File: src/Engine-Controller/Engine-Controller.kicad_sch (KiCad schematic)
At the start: 20 parts, among them J2 Jumper_NO, P3 3220-20-0200-00, U1 STM32H750VBTx, Y1 ECS-240-18-33-JGN-TR

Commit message: routed rev4
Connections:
- net NOZ_CONT: now also U1.38 (PE8); no longer U1.39 (PE9)
- net SP_CONT: now also U1.39 (PE9); no longer U1.38 (PE8)
- net SWCLK: now also R18.1
- net SWDIO: no longer R18.1
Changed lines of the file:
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@@
   (junction (at 248.285 140.97) (diameter 0) (color 0 0 0 0)
   )
+  (junction (at 201.295 117.475) (diameter 0) (color 0 0 0 0)
+  )
   (junction (at 204.47 145.415) (diameter 0) (color 0 0 0 0)
-  )
-  (junction (at 201.295 112.395) (diameter 0) (color 0 0 0 0)
   )
   (junction (at 32.385 41.91) (diameter 0) (color 0 0 0 0)
@@
     (stroke (width 0) (type default) (color 0 0 0 0))
   )
+  (wire (pts (xy 91.44 62.23) (xy 95.25 62.23))
+    (stroke (width 0) (type default) (color 0 0 0 0))
+  )
   (wire (pts (xy 91.44 39.37) (xy 95.25 39.37))
     (stroke (width 0) (type default) (color 0 0 0 0))
@@
     (stroke (width 0) (type default) (color 0 0 0 0))
   )
+  (wire (pts (xy 201.295 117.475) (xy 191.135 117.475))
+    (stroke (width 0) (type default) (color 0 0 0 0))
+  )
   (wire (pts (xy 31.115 127) (xy 34.29 127))
     (stroke (width 0) (type default) (color 0 0 0 0))
   )
-  (wire (pts (xy 91.44 62.23) (xy 95.25 62.23))
-    (stroke (width 0) (type default) (color 0 0 0 0))
-  )
   (polyline (pts (xy 172.085 116.205) (xy 115.57 116.205))
     (stroke (width 0) (type default) (color 0 0 0 0))
@@
     (stroke (width 0) (type default) (color 0 0 0 0))
   )
-  (wire (pts (xy 201.295 109.22) (xy 201.295 112.395))
+  (wire (pts (xy 91.44 59.69) (xy 95.25 59.69))
     (stroke (width 0) (type default) (color 0 0 0 0))
   )
@@
     (stroke (width 0) (type default) (color 0 0 0 0))
   )
-  (wire (pts (xy 207.01 112.395) (xy 201.295 112.395))
+  (wire (pts (xy 193.04 112.395) (xy 207.01 112.395))
     (stroke (width 0) (type default) (color 0 0 0 0))
   )
@@
     (stroke (width 0) (type default) (color 0 0 0 0))
   )
+  (wire (pts (xy 201.295 109.22) (xy 201.295 117.475))
+    (stroke (width 0) (type default) (color 0 0 0 0))
+  )
   (wire (pts (xy 32.385 46.99) (xy 32.385 49.53))
     (stroke (width 0) (type default) (color 0 0 0 0))
@@
     (stroke (width 0) (type default) (color 0 0 0 0))
   )
-  (wire (pts (xy 201.295 112.395) (xy 193.04 112.395))
-    (stroke (width 0) (type default) (color 0 0 0 0))
-  )
   (wire (pts (xy 91.44 69.85) (xy 95.25 69.85))
     (stroke (width 0) (type default) (color 0 0 0 0))
@@
     (stroke (width 0) (type default) (color 0 0 0 0))
   )
-  (wire (pts (xy 91.44 59.69) (xy 95.25 59.69))
-    (stroke (width 0) (type default) (color 0 0 0 0))
-  )
   (wire (pts (xy 31.115 74.93) (xy 34.29 74.93))
     (stroke (width 0) (type default) (color 0 0 0 0))
@@
     (stroke (width 0) (type default) (color 0 0 0 0))
   )
-  (wire (pts (xy 207.01 117.475) (xy 191.135 117.475))
+  (wire (pts (xy 207.01 117.475) (xy 201.295 117.475))
     (stroke (width 0) (type default) (color 0 0 0 0))
   )
@@
     )
   )
-  (global_label "SP_CONT" (shape input) (at 95.25 59.69 0) (fields_autoplaced)
-    (effects (font (size 1.27 1.27)) (justify left))
-    (property "Intersheet References" "${INTERSHEET_REFS}" (id 0) (at -43.18 5.08 0)
+  (global_label "SP_CONT" (shape input) (at 95.25 62.23 0) (fields_autoplaced)
+    (effects (font (size 1.27 1.27)) (justify left))
+    (property "Intersheet References" "${INTERSHEET_REFS}" (id 0) (at -43.18 7.62 0)
       (effects (font (size 1.27 1.27)) hide)
     )
@@
     )
   )
-  (global_label "NOZ_CONT" (shape input) (at 95.25 62.23 0) (fields_autoplaced)
-    (effects (font (size 1.27 1.27)) (justify left))
-    (property "Intersheet References" "${INTERSHEET_REFS}" (id 0) (at -43.18 5.08 0)
+  (global_label "NOZ_CONT" (shape input) (at 95.25 59.69 0) (fields_autoplaced)
+    (effects (font (size 1.27 1.27)) (justify left))
+    (property "Intersheet References" "${INTERSHEET_REFS}" (id 0) (at -43.18 2.54 0)
       (effects (font (size 1.27 1.27)) hide)
     )
@@
       (reference "#PWR0111") (unit 1) (value "Earth") (footprint "")
     )
+    (path "/d060135e-4b32-4403-ae1a-9301174376e1/88a7fee1-d900-4f58-a89f-e3298c086652"
+      (reference "#PWR0112") (unit 1) (value "Earth") (footprint "")
+    )
+    (path "/d060135e-4b32-4403-ae1a-9301174376e1/6d73f78e-83d1-4097-9135-98d5318ce286"
+      (reference "#PWR0113") (unit 1) (value "Earth") (footprint "")
+    )
     (path "/00000000-0000-0000-0000-0000610156a4"

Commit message: minor lib file changes
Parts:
- C8: value 0.1u -> 0.1uF
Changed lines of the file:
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@@
       (effects (font (size 1.27 1.27)) (justify left))
     )
-    (property "Value" "0.1u" (id 1) (at 135.3312 43.053 90)
+    (property "Value" "0.1uF" (id 1) (at 135.3312 43.053 90)
       (effects (font (size 1.27 1.27)) (justify left))
     )
@@
     )
     (path "/00000000-0000-0000-0000-000060de014c"
-      (reference "C8") (unit 1) (value "0.1u") (footprint "Engine-Controller:CAP_0603")
+      (reference "C8") (unit 1) (value "0.1uF") (footprint "Engine-Controller:CAP_0603")
     )
     (path "/00000000-0000-0000-0000-000060d7f309/0ec16f76-8a15-42e8-be61-e23900423f9a"
-      (reference "C9") (unit 1) (value "0.1u") (footprint "Engine-Controller:CAP_0603")
+      (reference "C9") (unit 1) (value "0.1uF") (footprint "Engine-Controller:CAP_0603")
     )
     (path "/00000000-0000-0000-0000-000060d7f309/4d2ae88c-b6ef-4cb6-b179-76f9053f5b7e"
@@
     )
     (path "/00000000-0000-0000-0000-000060d7f309/3a31ced4-1e7b-42c6-a2f1-fe4d16c32e29"
-      (reference "C11") (unit 1) (value "0.1u") (footprint "Engine-Controller:CAP_0603")
+      (reference "C11") (unit 1) (value "0.1uF") (footprint "Engine-Controller:CAP_0603")
     )
     (path "/00000000-0000-0000-0000-000060d7f309/1a1199eb-a7b0-4740-b190-e23949bfc7ec"
@@
     )
     (path "/00000000-0000-0000-0000-000060d7f309/e0ce634b-7c1d-4a97-89dc-87b6beef3d86"
-      (reference "C13") (unit 1) (value "0.1u") (footprint "Engine-Controller:CAP_0603")
+      (reference "C13") (unit 1) (value "0.1uF") (footprint "Engine-Controller:CAP_0603")
     )
     (path "/00000000-0000-0000-0000-000060d7f309/af637304-63ec-4ca0-9646-3e51f519efcf"
-      (reference "C14") (unit 1) (value "0.1u") (footprint "Engine-Controller:CAP_0603")
+      (reference "C14") (unit 1) (value "0.1uF") (footprint "Engine-Controller:CAP_0603")
     )
     (path "/00000000-0000-0000-0000-000060d7f309/00000000-0000-0000-0000-000060fd414b"
@@
     )
     (path "/00000000-0000-0000-0000-000060d7f309/c172997f-ac8e-44a5-a2ba-3e4cc4d99b9c"
-      (reference "C21") (unit 1) (value "0.1u") (footprint "Engine-Controller:CAP_0603")
+      (reference "C21") (unit 1) (value "0.1uF") (footprint "Engine-Controller:CAP_0603")
     )
     (path "/00000000-0000-0000-0000-000060d7f309/07894ac2-4d7e-4947-975c-a4f4124bdd22"
-      (reference "C22") (unit 1) (value "0.1u") (footprint "Engine-Controller:CAP_0603")
+      (reference "C22") (unit 1) (value "0.1uF") (footprint "Engine-Controller:CAP_0603")
     )
     (path "/00000000-0000-0000-0000-000060d7f309/66f033d4-7f4d-4d8b-8047-3c7c415b0219"
@@
     )
     (path "/9f3f32e1-1873-42fa-9cca-aa278e3c01ec/1843fcc5-48c4-4583-ad54-97557638cc54"
-      (reference "R6") (unit 1) (value "1k") (footprint "Engine-Controller:RES_0603")
+      (reference "R6") (unit 1) (value "10k") (footprint "Engine-Controller:RES_0603")
     )
     (path "/9f3f32e1-1873-42fa-9cca-aa278e3c01ec/72789c74-f9fc-44e0-856f-c74436508409"

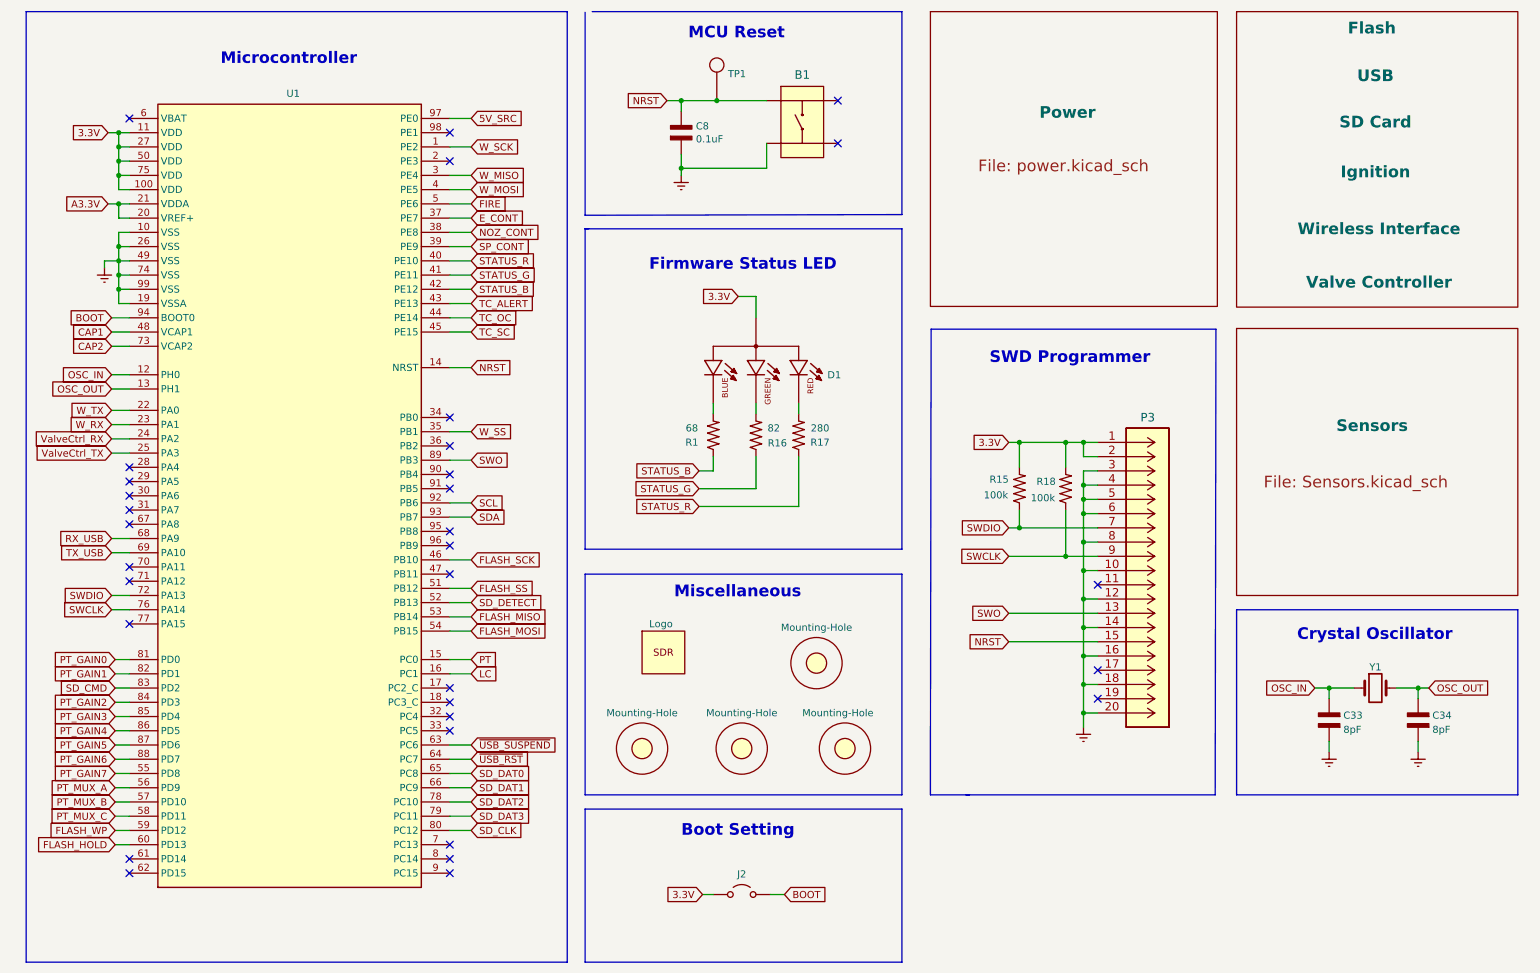
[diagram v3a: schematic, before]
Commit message: created rev5 schematic, added USB detection, updated PT readout circuits
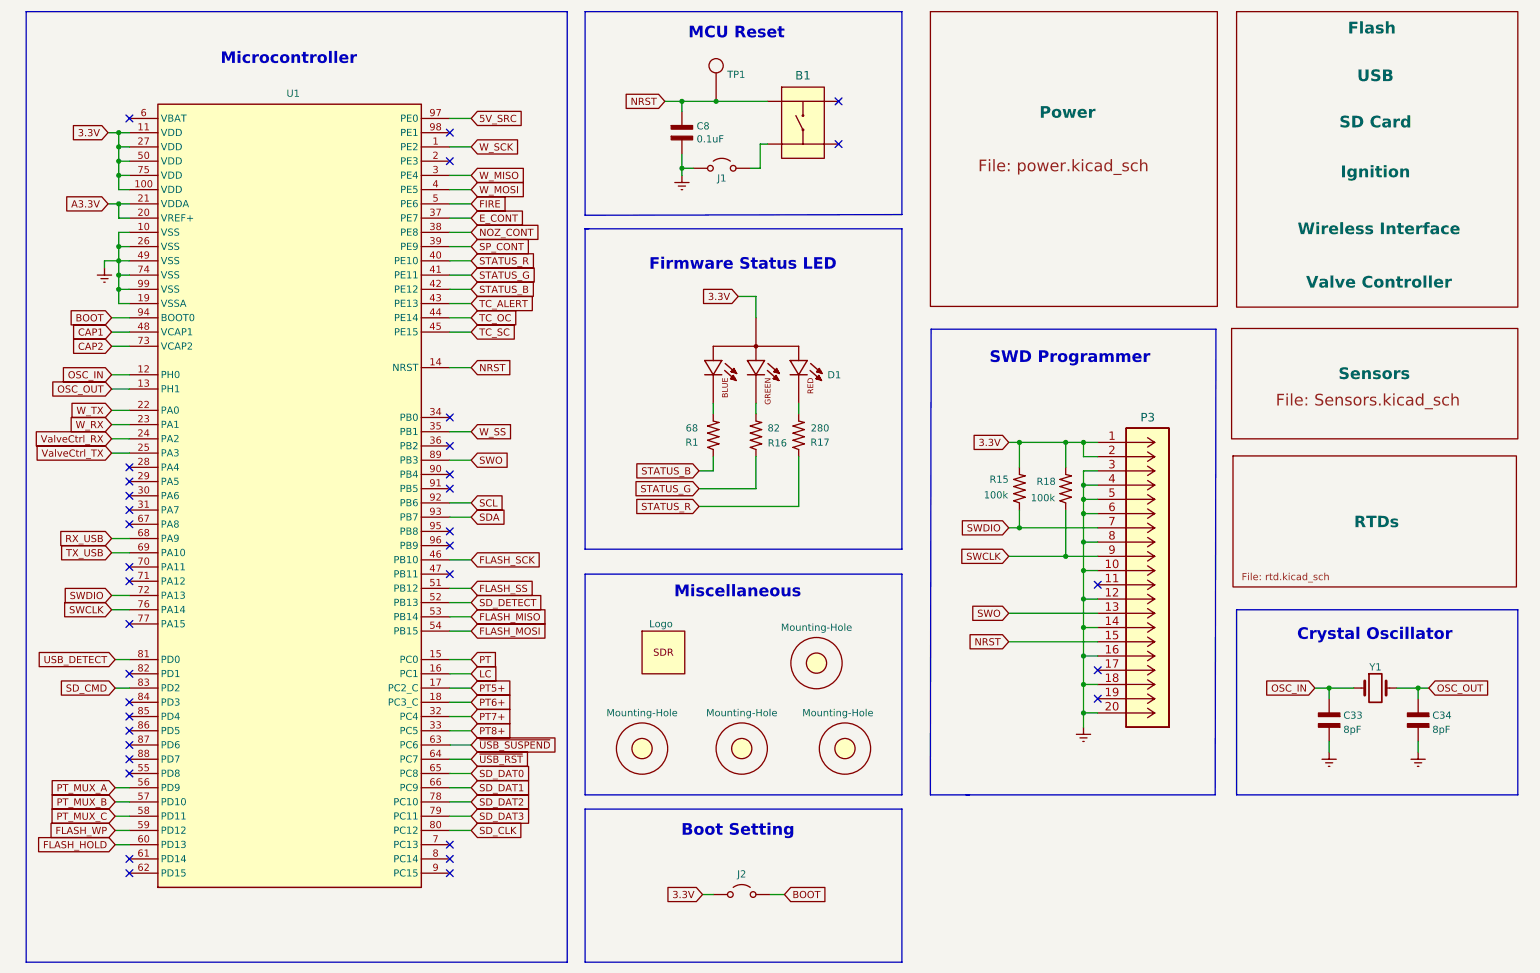
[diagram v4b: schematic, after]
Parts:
- added J1: Jumper_NO, symbol Engine-Controller:Jumper_NO
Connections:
- net Earth: now also J1.1 (A); no longer B1.1
- net PT5+: now reaches U1.17 (PC2_C)
- net PT6+: now reaches U1.18 (PC3_C)
- net PT7+: now reaches U1.32 (PC4)
- net PT8+: now reaches U1.33 (PC5)
- net PT_GAIN0 renamed USB_DETECT
- net PT_GAIN1: no longer names the net of U1.82 (PD1)
- net PT_GAIN2: no longer names the net of U1.84 (PD3)
- net PT_GAIN3: no longer names the net of U1.85 (PD4)
- net PT_GAIN4: no longer names the net of U1.86 (PD5)
- net PT_GAIN5: no longer names the net of U1.87 (PD6)
- net PT_GAIN6: no longer names the net of U1.88 (PD7)
- net PT_GAIN7: no longer names the net of U1.55 (PD8)
- new net: B1.1, J1.2 (B)
- no-connect marks 32 -> 35
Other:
- added sheet RTDs (rtd.kicad_sch)

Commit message: completed rev 5.0 layout
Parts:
- J1: footprint (none) -> Engine-Controller:Jumper-NO
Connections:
- net FIRE: now also U1.3 (PE4); no longer U1.5 (PE6)
- net W_MISO: now also U1.4 (PE5); no longer U1.3 (PE4)
- net W_MOSI: now also U1.5 (PE6); no longer U1.4 (PE5)
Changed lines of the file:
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@@
+    (stroke (width 0) (type default))
+  )
+  (polyline (pts (xy 172.085 59.055) (xy 172.085 116.205))
+    (stroke (width 0) (type default))
+  )
+  (wire (pts (xy 31.75 168.91) (xy 34.29 168.91))
+    (stroke (width 0) (type default))
+  )
+  (wire (pts (xy 91.44 44.45) (xy 95.25 44.45))
+    (stroke (width 0) (type default))
+  )
+  (wire (pts (xy 31.115 116.84) (xy 34.29 116.84))
+    (stroke (width 0) (type default))
+  )
+  (polyline (pts (xy 15.875 20.32) (xy 112.395 20.32))
+    (stroke (width 0) (type default))
+  )
+  (polyline (pts (xy 115.57 162.56) (xy 172.085 162.56))
+    (stroke (width 0) (type default))
+  )
+  (polyline (pts (xy 281.94 127) (xy 281.94 160.02))
+    (stroke (width 0) (type default))
+  )
+  (polyline (pts (xy 177.165 153.67) (xy 177.292 76.962))
+    (stroke (width 0) (type default))
+  )
+  (polyline (pts (xy 281.94 160.02) (xy 231.775 160.02))
+    (stroke (width 0) (type default))
+  )
+  (wire (pts (xy 31.75 158.75) (xy 34.29 158.75))
+    (stroke (width 0) (type default))
+  )
+  (wire (pts (xy 204.47 140.335) (xy 207.01 140.335))
+    (stroke (width 0) (type default))
+  )
+  (polyline (pts (xy 115.57 120.65) (xy 172.085 120.65))
+    (stroke (width 0) (type default))
+  )
+  (wire (pts (xy 204.47 147.955) (xy 204.47 145.415))
+    (stroke (width 0) (type default))
+  )
+  (wire (pts (xy 207.01 104.775) (xy 204.47 104.775))
+    (stroke (width 0) (type default))
+  )
+  (wire (pts (xy 91.44 62.23) (xy 95.25 62.23))
+    (stroke (width 0) (type default))
+  )
+  (wire (pts (xy 91.44 39.37) (xy 95.25 39.37))
+    (stroke (width 0) (type default))
+  )
+  (wire (pts (xy 264.16 150.495) (xy 264.16 152.4))
+    (stroke (width 0) (type default))
+  )
+  (wire (pts (xy 31.75 135.89) (xy 34.29 135.89))
+    (stroke (width 0) (type default))
+  )
+  (polyline (pts (xy 115.57 160.02) (xy 115.57 120.65))
+    (stroke (width 0) (type default))
+  )
+  (polyline (pts (xy 231.775 127) (xy 231.775 160.02))
+    (stroke (width 0) (type default))
+  )
+  (wire (pts (xy 204.47 120.015) (xy 207.01 120.015))
+    (stroke (width 0) (type default))
+  )
+  (wire (pts (xy 201.295 117.475) (xy 191.135 117.475))
+    (stroke (width 0) (type default))
+  )
+  (wire (pts (xy 31.115 127) (xy 34.29 127))
+    (stroke (width 0) (type default))
+  )
+  (polyline (pts (xy 172.085 116.205) (xy 115.57 116.205))
     (stroke (width 0) (type default))
   )
@@
     (stroke (width 0) (type default))
   )
-  (polyline (pts (xy 172.085 59.055) (xy 172.085 116.205))
-    (stroke (width 0) (type default))
-  )
-  (wire (pts (xy 31.75 168.91) (xy 34.29 168.91))
-    (stroke (width 0) (type default))
-  )
-  (wire (pts (xy 91.44 44.45) (xy 95.25 44.45))
-    (stroke (width 0) (type default))
-  )
-  (wire (pts (xy 31.115 116.84) (xy 34.29 116.84))
-    (stroke (width 0) (type default))
-  )
-  (polyline (pts (xy 15.875 20.32) (xy 112.395 20.32))
-    (stroke (width 0) (type default))
-  )
-  (polyline (pts (xy 115.57 162.56) (xy 172.085 162.56))
-    (stroke (width 0) (type default))
-  )
-  (polyline (pts (xy 281.94 127) (xy 281.94 160.02))
-    (stroke (width 0) (type default))
-  )
-  (polyline (pts (xy 177.165 153.67) (xy 177.292 76.962))
-    (stroke (width 0) (type default))
-  )
-  (polyline (pts (xy 281.94 160.02) (xy 231.775 160.02))
-    (stroke (width 0) (type default))
-  )
-  (wire (pts (xy 31.75 158.75) (xy 34.29 158.75))
-    (stroke (width 0) (type default))
-  )
-  (wire (pts (xy 204.47 140.335) (xy 207.01 140.335))
-    (stroke (width 0) (type default))
-  )
-  (polyline (pts (xy 115.57 120.65) (xy 172.085 120.65))
-    (stroke (width 0) (type default))
-  )
-  (wire (pts (xy 204.47 147.955) (xy 204.47 145.415))
-    (stroke (width 0) (type default))
-  )
-  (wire (pts (xy 207.01 104.775) (xy 204.47 104.775))
-    (stroke (width 0) (type default))
-  )
-  (wire (pts (xy 91.44 62.23) (xy 95.25 62.23))
-    (stroke (width 0) (type default))
-  )
-  (wire (pts (xy 91.44 39.37) (xy 95.25 39.37))
-    (stroke (width 0) (type default))
-  )
-  (wire (pts (xy 264.16 150.495) (xy 264.16 152.4))
-    (stroke (width 0) (type default))
-  )
-  (wire (pts (xy 31.75 135.89) (xy 34.29 135.89))
-    (stroke (width 0) (type default))
-  )
-  (polyline (pts (xy 115.57 160.02) (xy 115.57 120.65))
-    (stroke (width 0) (type default))
-  )
-  (polyline (pts (xy 231.775 127) (xy 231.775 160.02))
-    (stroke (width 0) (type default))
-  )
-  (wire (pts (xy 204.47 120.015) (xy 207.01 120.015))
-    (stroke (width 0) (type default))
-  )
-  (wire (pts (xy 201.295 117.475) (xy 191.135 117.475))
-    (stroke (width 0) (type default))
-  )
-  (wire (pts (xy 31.115 127) (xy 34.29 127))
-    (stroke (width 0) (type default))
-  )
-  (polyline (pts (xy 172.085 116.205) (xy 115.57 116.205))
-    (stroke (width 0) (type default))
-  )
   (wire (pts (xy 31.75 163.83) (xy 34.29 163.83))
     (stroke (width 0) (type default))
@@
     (stroke (width 0) (type default))
   )
+  (wire (pts (xy 91.44 49.53) (xy 95.25 49.53))
+    (stroke (width 0) (type default))
+  )
   (wire (pts (xy 31.115 77.47) (xy 34.29 77.47))
     (stroke (width 0) (type default))
@@
     (stroke (width 0) (type default))
   )
-  (wire (pts (xy 91.44 49.53) (xy 95.25 49.53))
-    (stroke (width 0) (type default))
-  )
   (wire (pts (xy 91.44 110.49) (xy 95.25 110.49))
     (stroke (width 0) (type default))
@@
     (stroke (width 0) (type default))
   )
+  (wire (pts (xy 91.44 54.61) (xy 95.25 54.61))
+    (stroke (width 0) (type default))
+  )
   (wire (pts (xy 148.59 177.8) (xy 151.13 177.8))
     (stroke (width 0) (type default))
@@
   )
   (polyline (pts (xy 115.57 116.205) (xy 115.57 59.055))
-    (stroke (width 0) (type default))
-  )
-  (wire (pts (xy 91.44 54.61) (xy 95.25 54.61))
     (stroke (width 0) (type default))
   )
@@
     )
   )
-  (global_label "W_MISO" (shape input) (at 95.25 49.53 0) (fields_autoplaced)
-    (effects (font (size 1.27 1.27)) (justify left))
-    (property "Intersheetrefs" "${INTERSHEET_REFS}" (at 104.5894 49.6094 0)
-      (effects (font (size 1.27 1.27)) (justify left) hide)
-    )
-  )
-  (global_label "W_MOSI" (shape input) (at 95.25 52.07 0) (fields_autoplaced)
+  (global_label "W_MISO" (shape input) (at 95.25 52.07 0) (fields_autoplaced)
     (effects (font (size 1.27 1.27)) (justify left))
     (property "Intersheetrefs" "${INTERSHEET_REFS}" (at 104.5894 52.1494 0)
@@
     )
   )
+  (global_label "W_MOSI" (shape input) (at 95.25 54.61 0) (fields_autoplaced)
+    (effects (font (size 1.27 1.27)) (justify left))
+    (property "Intersheetrefs" "${INTERSHEET_REFS}" (at 104.5894 54.6894 0)
+      (effects (font (size 1.27 1.27)) (justify left) hide)
+    )
+  )
   (global_label "SWDIO" (shape input) (at 31.115 124.46 180) (fields_autoplaced)
     (effects (font (size 1.27 1.27)) (justify right))
@@
     )
   )
-  (global_label "FIRE" (shape input) (at 95.25 54.61 0) (fields_autoplaced)
-    (effects (font (size 1.27 1.27)) (justify left))
-    (property "Intersheetrefs" "${INTERSHEET_REFS}" (at -43.18 5.08 0)
+  (global_label "FIRE" (shape input) (at 95.25 49.53 0) (fields_autoplaced)
+    (effects (font (size 1.27 1.27)) (justify left))
+    (property "Intersheetrefs" "${INTERSHEET_REFS}" (at -43.18 0 0)
       (effects (font (size 1.27 1.27)) hide)
     )
@@
       (effects (font (size 1.27 1.27)) hide)
     )
-    (property "Footprint" "" (at 139.954 48.26 0)
-      (effects (font (size 1.27 1.27)) hide)
-    )
+    (property "Footprint" "Engine-Controller:Jumper-NO" (at 139.954 48.26 0)
+      (effects (font (size 1.27 1.27)) hide)
+    )
